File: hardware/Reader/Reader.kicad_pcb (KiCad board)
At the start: 4 copper layers, 134 parts

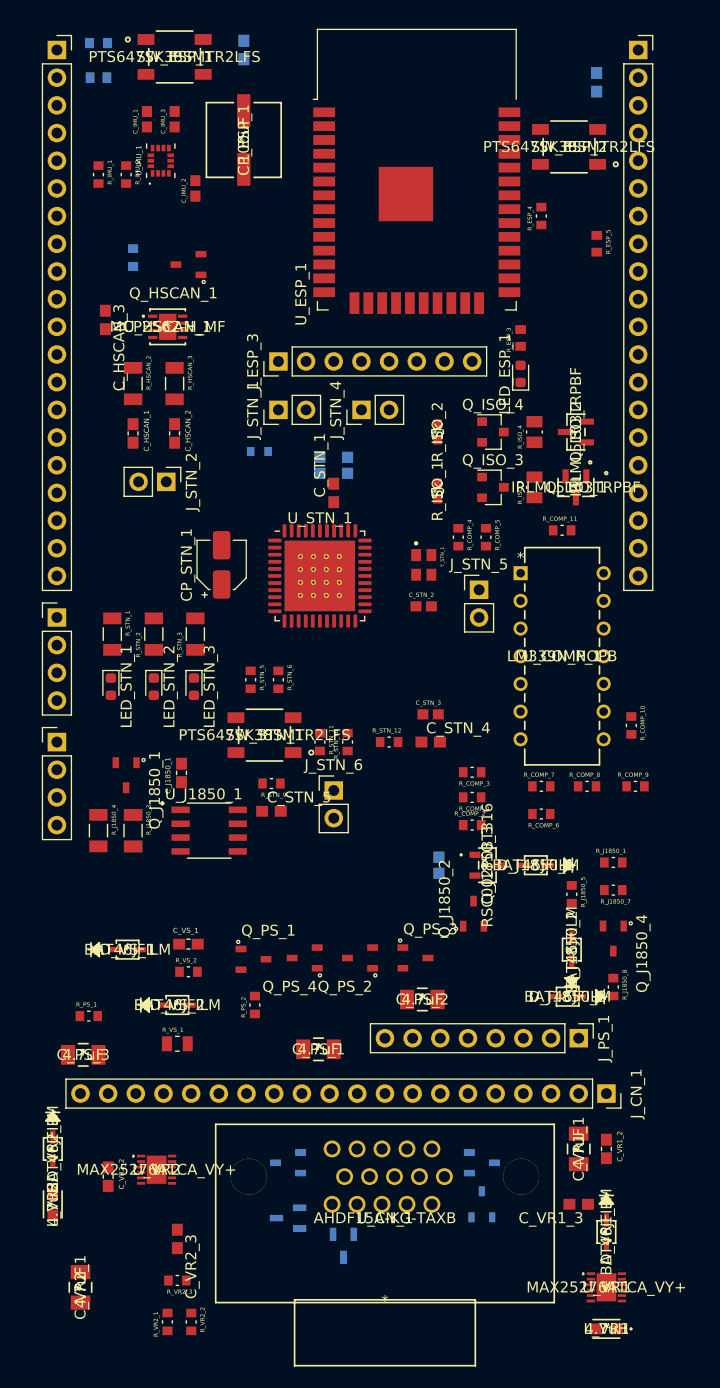
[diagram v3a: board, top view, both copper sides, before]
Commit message: Updated schematic and gerber to v0.0.05. Added ESP32. Removed MS CAN and SW CAN Transceivers. Added silkscreen text to header pins. Improved readability
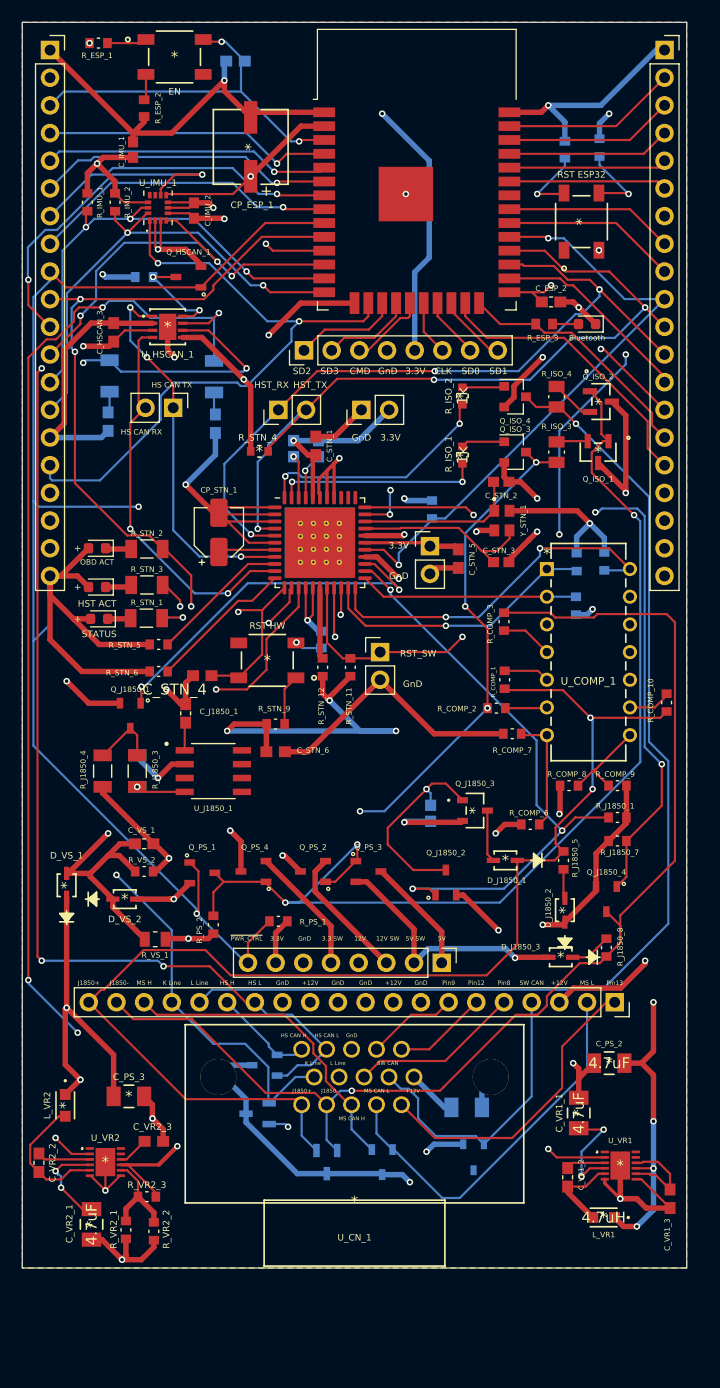
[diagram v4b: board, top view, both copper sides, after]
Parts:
- removed C_IMU_3: 100nF, footprints:CAPC1608X90N
- removed D_VR1_1, D_VR2_1: BAT46JFILM, footprints:BAT46JFILM
- removed J_OBD_1, J_OBD_2: Header_Pin_4, Connector_PinHeader_2.54mm:PinHeader_1x04_P2.54mm_Vertical
- added C_STN_4: 1uF, footprints:0603, F.Cu at (85.1, 115.8)
- added R_STN_10: 500, footprints:RESC1508X55N, B.Cu at (96.0, 112.5)
- C_ESP_2, R_ESP_1, R_ESP_2, R_STN_4: moved to F.Cu
- C_HSCAN_1, C_HSCAN_2, C_PS_1, R_COMP_11, R_COMP_4, R_COMP_5, R_ESP_4, R_ESP_5, R_HSCAN_2, R_HSCAN_3: moved to B.Cu
- LED_ESP_1: value LED -> Bluetooth Status
- R_STN_13: renamed from R_STN_12; moved to B.Cu
- moved R_STN_13 21.7 mm to (106.2, 100.6), turned to 270 degrees
- moved C_ESP_2 20.6 mm to (117.1, 81.5), turned to 0 degrees
- moved R_PS_1 19.5 mm to (92.1, 138.4), turned to 180 degrees
- moved C_PS_2 18.1 mm to (122.4, 151.4)
- moved C_STN_5 17.0 mm to (108.6, 105.1), turned to 270 degrees
- moved C_STN_3 15.4 mm to (112.5, 105.4)
- moved C_PS_1 14.6 mm to (109.3, 155.4)
- moved J_PS_1 14.4 mm to (107.1, 142.2)
- moved R_COMP_3 14.1 mm to (112.8, 110.9), turned to 90 degrees
- moved LED_STN_2 13.7 mm to (75.4, 104.1), turned to 180 degrees
- moved C_STN_2 13.5 mm to (112.5, 98.0), turned to 180 degrees
- moved J_STN_6 13.4 mm to (101.4, 113.7)
- moved LED_STN_3 12.8 mm to (75.4, 107.7), turned to 180 degrees
- moved R_COMP_4 12.5 mm to (119.4, 109.4), turned to 90 degrees
- moved U_VR1 11.2 mm to (123.4, 160.8)
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- renumbered C_STN_4 to C_STN_5, C_STN_5 to C_STN_6, R_STN_10 to R_STN_11, R_STN_11 to R_STN_12
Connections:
- net /OBDII Interpreter/OBDII Chip/STATUS_LED renamed Net-(R_STN_1-Pad2)
- net /OBDII Interpreter/OBDII Chip/~HOST_ACT_LED~ renamed Net-(R_STN_3-Pad2)
- J_ESP_1 pad 10: /Host/ESP32/ESP32_Pin10 -> /Host/~RESET_OBD_HW~
- J_ESP_1 pad 18: +5V_SW -> (no net)
- J_ESP_1 pad 20: +5V -> +3V3
- J_ESP_1 pad 9: /Host/ESP32/ESP32_Pin9 -> /Host/~PWR_CTRL~
- J_ESP_2 pad 13: /Host/~PWR_CTRL~ -> /Host/ESP32/ESP32_Pin26
- J_ESP_2 pad 15: /OBDII Interpreter/RESET_OBD_SW -> /Host/ESP32/ESP32_Pin24
- J_ESP_2 pad 16: /Host/~RESET_OBD_HW~ -> /Host/ESP32/ESP32_Pin23
- J_ESP_2 pad 17: +3V3 -> +5V
- J_ESP_2 pad 18: +3.3V_SW -> (no net)
- J_ESP_2 pad 9: /Host/ESP32/ESP32_Pin30 -> /Host/~RESET_OBD_SW~
- J_STN_6 pad 1: /OBDII Interpreter/RESET_OBD_SW -> /Host/~RESET_OBD_SW~
- L_VR1 pad 1: Net-(D_VR1_1-Pad2) -> +5V
- L_VR2 pad 1: Net-(D_VR2_1-Pad2) -> +3V3
- R_ESP_3 pad 2: /OBDII Interpreter/RESET_OBD_SW -> /Host/ESP32/ESP32_Pin24
- R_STN_11 pad 2: /OBDII Interpreter/RESET_OBD_SW -> /Host/~RESET_OBD_SW~
- R_VR2_3 pad 1: Net-(D_VR2_1-Pad2) -> +3V3
- SW_STN_1 pad 3: Pin4_GnD_Chassis -> Net-(R_STN_10-Pad1)
- U_ESP_1 pad 10: /Host/ESP32/ESP32_Pin10 -> /Host/~RESET_OBD_HW~
- U_ESP_1 pad 23: /Host/~RESET_OBD_HW~ -> /Host/ESP32/ESP32_Pin23
- U_ESP_1 pad 24: /OBDII Interpreter/RESET_OBD_SW -> /Host/ESP32/ESP32_Pin24
- U_ESP_1 pad 26: /Host/~PWR_CTRL~ -> /Host/ESP32/ESP32_Pin26
- U_ESP_1 pad 30: /Host/ESP32/ESP32_Pin30 -> /Host/~RESET_OBD_SW~
- U_ESP_1 pad 9: /Host/ESP32/ESP32_Pin9 -> /Host/~PWR_CTRL~
- U_STN_1 pad 18: /OBDII Interpreter/RESET_OBD_SW -> /Host/~RESET_OBD_SW~
- U_VR1 pad 9: Net-(D_VR1_1-Pad2) -> +5V
- U_VR2 pad 9: Net-(D_VR2_1-Pad2) -> +3V3
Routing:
- net Pin4_GnD_Chassis: track 0.00 -> 842.5 mm, vias 0 -> 31
- net +3V3: track 0.00 -> 577.8 mm, vias 0 -> 19
- net Pin16_Raw_+12V_Battery: track 0.00 -> 205.5 mm, vias 0 -> 6
- net +5V: track 0.00 -> 173.8 mm, vias 0 -> 5
- net /Host/~PWR_CTRL~: track 0.00 -> 150.6 mm, vias 0 -> 4
- net Pin15_ISO9141_L-Line: track 0.00 -> 123.3 mm, vias 0 -> 2
- net Pin6_ISO15765_CAN_BUS_High: track 0.00 -> 118.0 mm, vias 0 -> 4
- net Pin14_ISO15765_CAN_BUS_Low: track 0.00 -> 116.7 mm, vias 0 -> 5
- net Pin2_SAE_J1850_BUS+: track 0.00 -> 114.2 mm, vias 0 -> 2
- net Pin10_SAE_J1850_BUS-: track 0.00 -> 112.6 mm, vias 0 -> 1
- net Pin7_ISO9141_K-Line: track 0.00 -> 103.5 mm, vias 0 -> 5
- net /OBDII Interpreter/PWR_CTRL: track 0.00 -> 100.6 mm, vias 0 -> 3
- net /Host/~RESET_OBD_HW~: track 0.00 -> 81.8 mm, vias 0 -> 4
- net /Host/~RESET_OBD_SW~: track 0.00 -> 76.4 mm, vias 0 -> 3
- net /Host/HST_TX: track 0.00 -> 72.0 mm, vias 0 -> 3
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- added copper zone on In2.Cu, net +3V3
- added copper zone on B.Cu, net Pin4_GnD_Chassis
- added copper zone on F.Cu, net Pin4_GnD_Chassis
- added copper zone on In1.Cu, net Pin4_GnD_Chassis
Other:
- board outline added: 61 x 114.3 mm
- board text added: "CANtech | CANnect Reader v0.0.05"
- board text added: "Created by Choong Jin Ng | jin8383@gmail.com"
- board text added: "Published on 29 November 2020"

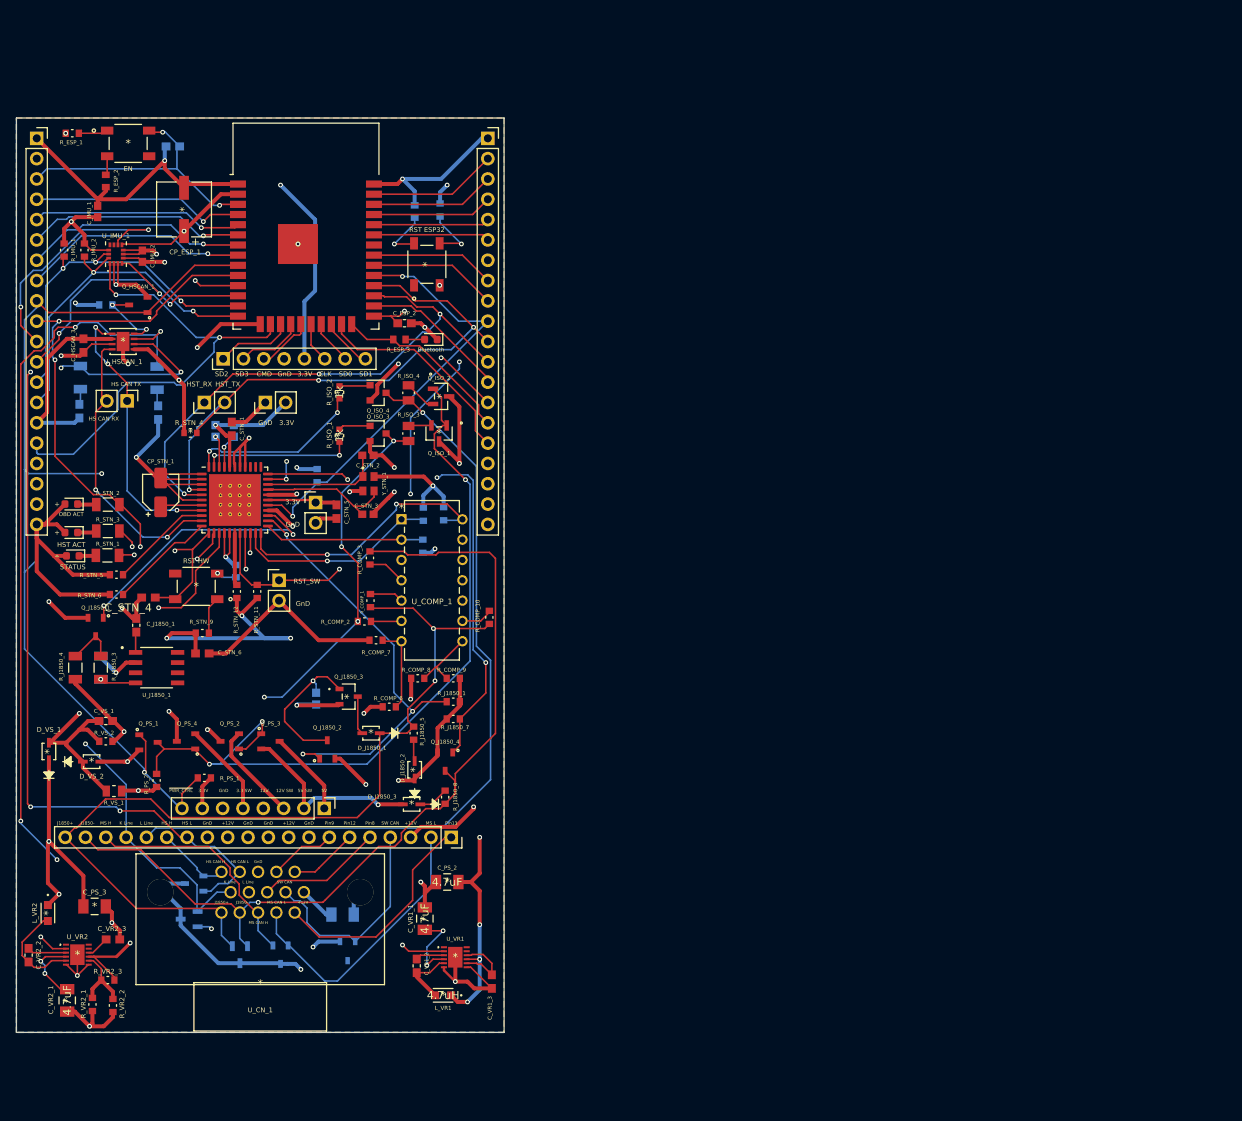
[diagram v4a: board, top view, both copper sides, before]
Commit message: Converted PCB design into a 2-layer PCB for v0.0.5b. Adjusted schematic to use header pins for connector
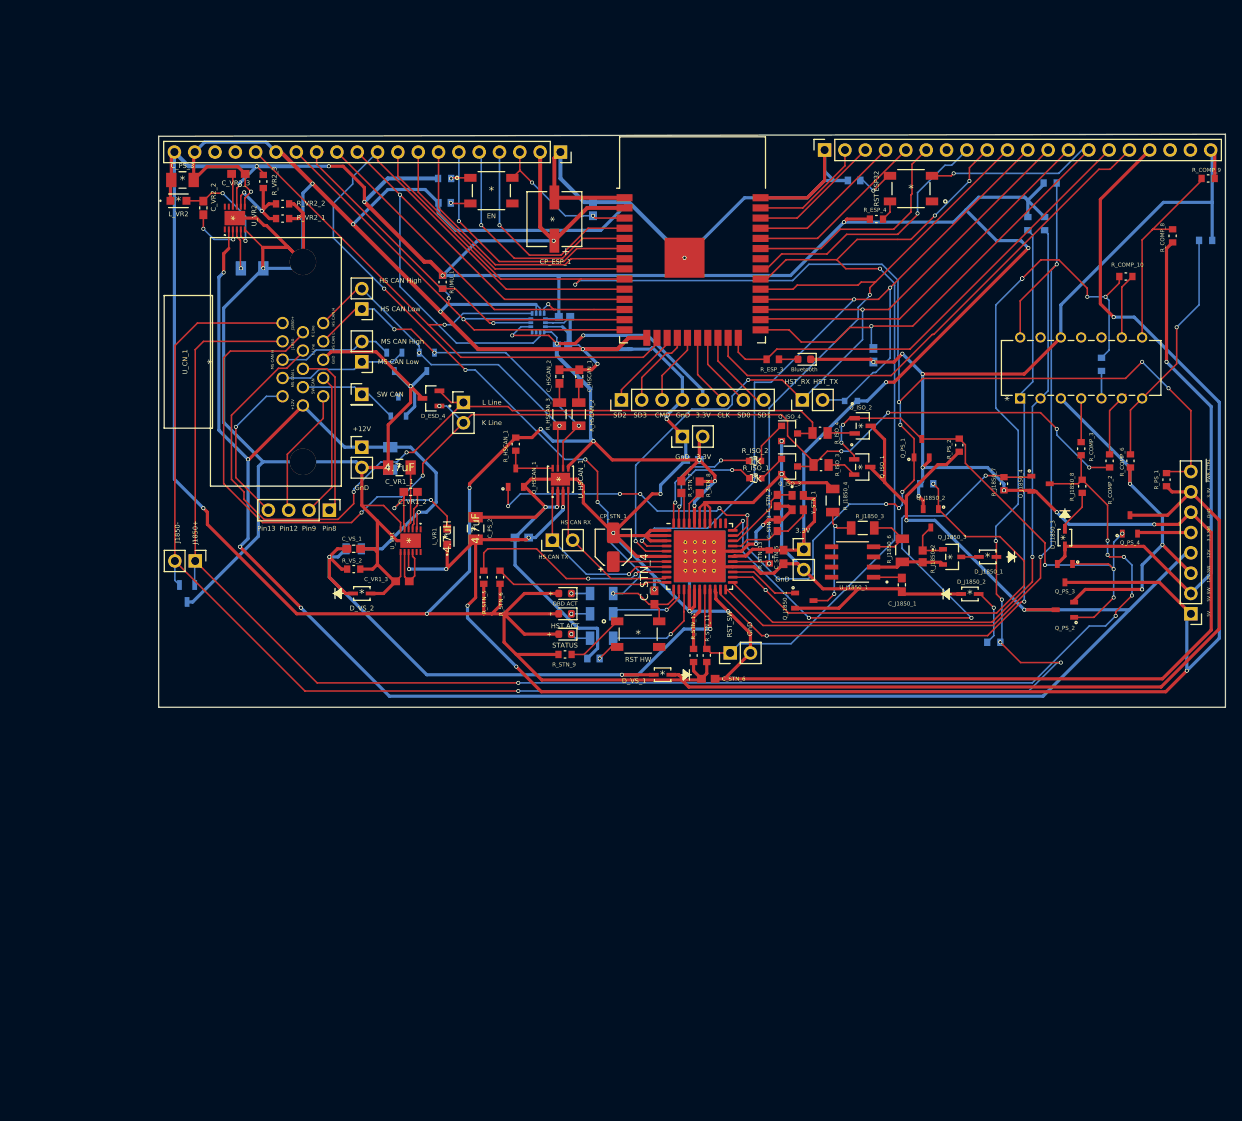
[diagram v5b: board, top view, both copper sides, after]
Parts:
- added J_CN_2: Header_Pin_2, Connector_PinHeader_2.54mm:PinHeader_1x02_P2.54mm_Vertical, F.Cu at (124.5, 91.4)
- added J_CN_3: Header_Pin_1, Connector_PinHeader_2.54mm:PinHeader_1x01_P2.54mm_Vertical, F.Cu at (111.8, 90.4)
- added J_CN_4: Header_Pin_2, Connector_PinHeader_2.54mm:PinHeader_1x02_P2.54mm_Vertical, F.Cu at (111.8, 86.4)
- added J_CN_5: Header_Pin_2, Connector_PinHeader_2.54mm:PinHeader_1x02_P2.54mm_Vertical, F.Cu at (111.8, 79.8)
- added J_CN_6: Header_Pin_2, Connector_PinHeader_2.54mm:PinHeader_1x02_P2.54mm_Vertical, F.Cu at (111.8, 97.0)
- added J_CN_7: Header_Pin_4, Connector_PinHeader_2.54mm:PinHeader_1x04_P2.54mm_Vertical, F.Cu at (107.7, 104.9)
- C_ESP_2, C_HSCAN_3, C_IMU_1, C_IMU_2, C_STN_1, C_VR2_1, R_COMP_1, R_COMP_7, R_ESP_1, R_ESP_2, R_IMU_2, R_J1850_1, R_J1850_5, R_STN_1, R_STN_2, R_STN_3, R_STN_4, R_VS_1, U_IMU_1: moved to B.Cu
- C_HSCAN_1, C_HSCAN_2, D_ESD_4, R_ESP_4, R_HSCAN_1, R_HSCAN_2, R_HSCAN_3, R_J1850_2, R_J1850_6, R_STN_13, R_STN_7, R_STN_8: moved to F.Cu
- J_CN_1: value 4157 -> Header_Pin_2; footprint Connector_PinSocket_2.54mm:PinSocket_1x20_P2.54mm_Vertical -> Connector_PinHeader_2.54mm:PinHeader_1x02_P2.54mm_Vertical
- moved R_PS_1 125.9 mm to (212.3, 101.1), turned to 90 degrees
- moved Q_PS_4 121.1 mm to (207.8, 106.7), turned to 90 degrees
- moved R_COMP_7 115.1 mm to (217.2, 71.2), turned to 0 degrees
- moved R_COMP_9 113.2 mm to (217.6, 63.4)
- moved J_PS_1 111.0 mm to (215.4, 117.9), turned to 180 degrees
- moved R_COMP_8 109.4 mm to (213.1, 70.6), turned to 90 degrees
- moved R_PS_2 108.7 mm to (186.4, 96.8)
- moved Q_PS_2 105.7 mm to (199.6, 117.3)
- moved Q_PS_1 103.4 mm to (181.7, 97.2), turned to 90 degrees
- moved R_VR2_2 102.4 mm to (101.9, 66.6), turned to 0 degrees
- moved R_VR2_3 101.7 mm to (99.4, 63.8), turned to 270 degrees
- moved Q_PS_3 101.5 mm to (199.6, 112.8), turned to 270 degrees
- moved R_J1850_6 101.3 mm to (179.3, 109.9), turned to 90 degrees
- moved R_VR2_1 101.1 mm to (101.9, 68.5), turned to 180 degrees
- moved R_COMP_6 97.6 mm to (207.8, 98.7), turned to 90 degrees
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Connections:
- J_CN_1 pad 1: Pin13 -> Pin10_SAE_J1850_BUS-
- J_CN_1 pad 2: Pin11_MS_CAN_Low -> Pin2_SAE_J1850_BUS+
- R_ESP_4 pad 1: +3V3 -> Net-(R_ESP_4-Pad1)
- R_ESP_4 pad 2: Net-(R_ESP_4-Pad2) -> +3V3
- R_ESP_5 pad 1: Net-(R_ESP_5-Pad1) -> Pin4_GnD_Chassis
- R_ESP_5 pad 2: Pin4_GnD_Chassis -> Net-(R_ESP_5-Pad2)
- SW_ESP_2 pad 2: Net-(R_ESP_5-Pad1) -> Net-(R_ESP_4-Pad1)
- SW_ESP_2 pad 4: Net-(R_ESP_4-Pad2) -> Net-(R_ESP_5-Pad2)
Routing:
- net Pin2_SAE_J1850_BUS+: track 114.2 -> 247.3 mm, vias 2 -> 9
- net +3V3: track 577.8 -> 665.1 mm, vias 19 -> 20
- net Pin10_SAE_J1850_BUS-: track 112.6 -> 194.5 mm, vias 1 -> 6
- net Pin16_Raw_+12V_Battery: track 205.5 -> 286.2 mm, vias 6 -> 7
- net /Host/~PWR_CTRL~: track 150.6 -> 231.0 mm, vias 4 -> 13
- net Pin4_GnD_Chassis: track 842.5 -> 916.8 mm, vias 31 -> 30
- net Pin6_ISO15765_CAN_BUS_High: track 118.0 -> 44.3 mm, vias 4 -> 2
- net /OBDII Interpreter/Comparator Transceiver/VPW_RX: track 33.7 -> 105.1 mm
- net Pin14_ISO15765_CAN_BUS_Low: track 116.7 -> 45.8 mm, vias 5 -> 3
- net /OBDII Interpreter/Comparator Transceiver/PWM_RX: track 20.1 -> 86.6 mm, vias 0 -> 1
- net /OBDII Interpreter/Comparator Transceiver/~ISO_RX~: track 25.7 -> 90.0 mm, vias 1 -> 2
- net +5V: track 173.8 -> 236.8 mm, vias 5 -> 8
- net Pin7_ISO9141_K-Line: track 103.5 -> 162.2 mm, vias 5 -> 7
- net /Host/ESP32/ESP32_Pin25: track 27.0 -> 75.4 mm, vias 3 -> 2
- net /Host/~RESET_OBD_HW~: track 81.8 -> 128.2 mm, vias 4 -> 5
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- removed copper zone on In2.Cu, net +3V3
- removed copper zone on B.Cu, net Pin4_GnD_Chassis
- removed copper zone on F.Cu, net Pin4_GnD_Chassis
- removed copper zone on In1.Cu, net Pin4_GnD_Chassis
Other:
- board size 61 x 114.3 mm -> 133.4 x 71.6 mm
- copper layers 4 -> 2
- net class Default: via_dia 0.6 -> 0.5
- net class Power: trace_width 0.5 -> 0.4; via_dia 0.6 -> 0.5
- rule via_min_size: 0.6 -> 0.5
- board text added: "CANtech | CANnect Reader v0.0.05b"
- board text added: "Published on 02 December 2020"
- board text removed: "CANtech | CANnect Reader v0.0.05"
- board text removed: "Published on 29 November 2020"

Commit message: Added keep-out area to ESP32 antenna. Updated silkscreen of Reader
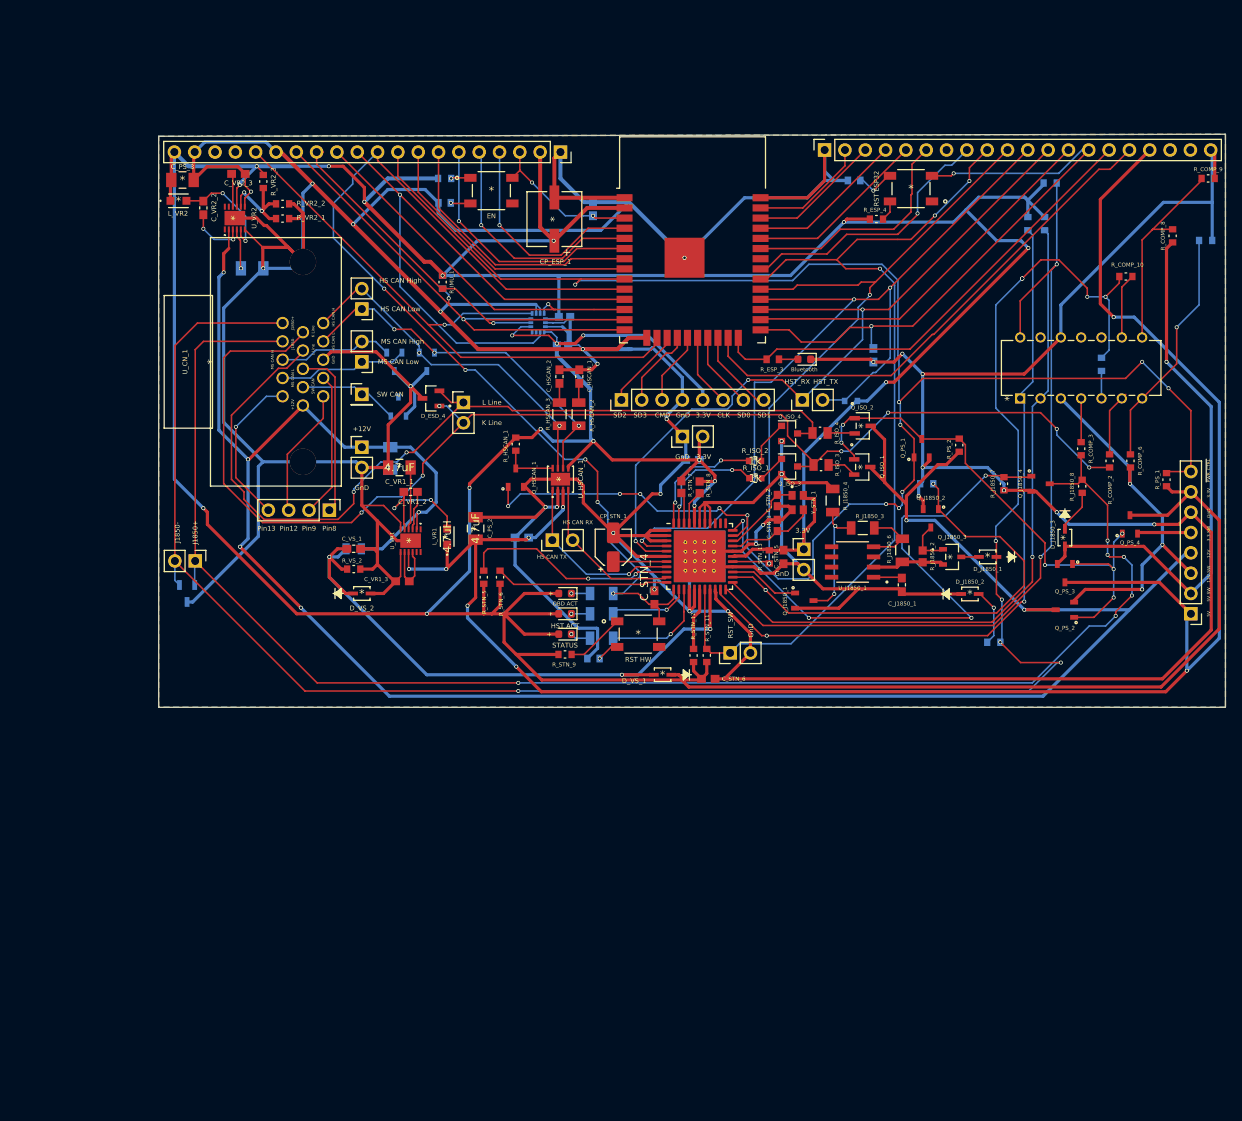
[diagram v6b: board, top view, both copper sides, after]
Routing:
- added copper zone on B.Cu, net Pin4_GnD_Chassis
- added copper zone on F.Cu, net Pin4_GnD_Chassis
